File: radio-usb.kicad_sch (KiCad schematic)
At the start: 236 parts, among them J1 Barrel_Jack, J10 Conn_Coaxial, J11 ACJS-MHDRM, J12 ACJS-MHDRM, J2 miniUSB, J3 15EDGRC-3.5-03P-14, J4 DB9_Female, J5 EEP_EN, J6 Mini-DIN-6, J7 EDAC 690-008-221-904, J8 DB9_Male, J9 Conn_Coaxial, Q1 BC846C, Q2 BC846, Q3 BC846, Q4 BC846, Q5 BC856, SW1 SW_Push_DPDT, SW2 SW_SPDT, SW3 SW_SPDT, SW4 SW_DIP_x04, SW5 SW_DIP_x04, SW6 SW_DPDT_x2, SW7 SW_SPDT, U1 L7805, U10 AP2171W, U11 TLP2662, U12 TLP2662, U13 MAX3232, U14 93CxxC, U15 PCM2902, U16 MIC5209-3.6YS, U17 FT2232HL, U18 PC817, U19 CRIYCHLEY9000, U2 24LC04, U20 PC817, U21 PC817, U22 CRIYCHLEY9000, U23 LMV358, U3 APX809_810-xxSA, U4 AP22814AW5, U5 AP22814AW5, U6 USB2514B_Bi, U7 LM1117-3.3, U8 TBA 1-0511, U9 4069, X1 MAB5SH, Y1 24MHz, Y2 12MHz, Y3 12M

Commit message: daily
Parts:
- removed C43: 1u, Capacitor_SMD:C_0805_2012Metric_Pad1.18x1.45mm_HandSolder, symbol Device:C
- removed F1: Polyfuse 100mA, Resistor_SMD:R_1210_3225Metric_Pad1.30x2.65mm_HandSolder, symbol Device:Polyfuse
- removed R56: 0, Resistor_SMD:R_0805_2012Metric_Pad1.20x1.40mm_HandSolder, symbol Device:R
- removed R71, R72, R73, R74: 2k2, Resistor_SMD:R_0805_2012Metric_Pad1.20x1.40mm_HandSolder, symbol Device:R
- removed RV1: 10k, potentiometers:Potentiometer_SRpassives_1028F, symbol Device:R_Potentiometer
- removed U16: MIC5209-3.6YS, Package_TO_SOT_SMD:SOT-223-3_TabPin2, symbol MIC5209:MIC5209-3.3YS
- removed U23: LMV358, Package_SO:TSSOP-8_4.4x3mm_P0.65mm, symbol Amplifier_Operational:LMV358
- added R69: 0, Resistor_SMD:R_0603_1608Metric_Pad0.98x0.95mm_HandSolder, symbol Device:R_Small
- added R70: DNP, Resistor_SMD:R_0603_1608Metric_Pad0.98x0.95mm_HandSolder, symbol Device:R_Small
- added U23: LMV321IDBVR, Package_TO_SOT_SMD:SOT-23-5_HandSoldering, symbol Amplifier_Operational:LMV321
- R78: renamed from R76; footprint Resistor_SMD:R_0805_2012Metric_Pad1.20x1.40mm_HandSolder -> Resistor_SMD:R_0603_1608Metric_Pad0.98x0.95mm_HandSolder
- renumbered C42 to C43, C44 to C45, C45 to C46, C46 to C47, C47 to C48, C48 to C49, C49 to C50, C50 to C51, C51 to C52, C52 to C53, C53 to C54, C54 to C55, C55 to C56, C56 to C57, C57 to C58, C58 to C59, C59 to C60, C60 to C61, C61 to C62, C62 to C63, C63 to C64, C64 to C65, R44 to R42, R46 to R43, R42 to R44, R43 to R45, R45 to R46, R69 to R71, R70 to R72, R75 to R77, R77 to R79, R78 to R80, R79 to R81
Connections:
- net AUD_VBUS: now also U23.5 (V+)
- net GND: now also R70.1, U23.2 (V-)
- net PTT_CTRL: now also D17.1 (K), D18.1 (K), D19.1 (K), D20.1 (K)
- net VD: now also C23.1, L3.2
- net at C62.1, R77.2: now also U23.4
- net at R71.1: now also U23.1 (+)
- net at R67.2, R68.2, R77.1: now also U23.3 (-)
- net at J11.T: now also R69.1, R70.2
- net at U22.P$1: now also R69.2
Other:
- moved on the sheet: C49

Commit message: all components placed
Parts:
- removed C65: 100n, Capacitor_SMD:C_0805_2012Metric_Pad1.18x1.45mm_HandSolder, symbol Device:C
- R35, R36, R37: footprint Resistor_SMD:R_0805_2012Metric_Pad1.20x1.40mm_HandSolder -> Resistor_SMD:R_0603_1608Metric_Pad0.98x0.95mm_HandSolder
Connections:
- net DCDC_OUT: now reaches C20.1, C22.2, L3.1, U8.4 (+VOUT)
- net DCDC_IN: now reaches C18.1, C19.1, L2.2, U8.2 (+VIN)
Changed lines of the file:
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@@
     (effects (font (size 1.27 1.27)) (justify left bottom))
   )
+  (label "DCDC_IN" (at 125.984 134.366 0)
+    (effects (font (size 1.27 1.27)) (justify left bottom))
+  )
   (label "H_AUD_USBD-" (at 216.154 136.906 90)
     (effects (font (size 1.27 1.27)) (justify left bottom))
@@
     (effects (font (size 1.27 1.27)) (justify left bottom))
   )
+  (label "DCDC_OUT" (at 165.354 134.366 0)
+    (effects (font (size 1.27 1.27)) (justify left bottom))
+  )
   (label "DP2+" (at 178.308 79.502 0)
     (effects (font (size 1.27 1.27)) (justify left bottom))
@@
     (effects (font (size 1.27 1.27)) (justify right))
   )
-  (hierarchical_label "AUD_VBUS" (shape input) (at 392.938 152.654 90)
-    (effects (font (size 1.27 1.27)) (justify left))
-  )
   (hierarchical_label "CAT_UART_RX" (shape input) (at 197.866 191.516 0)
     (effects (font (size 1.27 1.27)) (justify left))
@@
     (property "Reference" "R35" (id 0) (at 179.07 17.78 90))
     (property "Value" "620" (id 1) (at 179.07 19.4111 90))
-    (property "Footprint" "Resistor_SMD:R_0805_2012Metric_Pad1.20x1.40mm_HandSolder" (id 2) (at 179.07 23.368 90)
+    (property "Footprint" "Resistor_SMD:R_0603_1608Metric_Pad0.98x0.95mm_HandSolder" (id 2) (at 179.07 23.368 90)
       (effects (font (size 1.27 1.27)) hide)
     )
@@
       (effects (font (size 1.27 1.27)) hide)
     )
-    (property "Footprint" "Resistor_SMD:R_0805_2012Metric_Pad1.20x1.40mm_HandSolder" (id 2) (at 179.07 28.448 90)
+    (property "Footprint" "Resistor_SMD:R_0603_1608Metric_Pad0.98x0.95mm_HandSolder" (id 2) (at 179.07 28.448 90)
       (effects (font (size 1.27 1.27)) hide)
     )
@@
     (pin "1")
   )
-  (symbol (lib_id "power:GND") (at 392.938 160.274 0) (mirror y) (unit 1)
-    (in_bom yes) (on_board yes)
-    (property "Reference" "#PWR0156" (id 0) (at 392.938 166.624 0)
-      (effects (font (size 1.27 1.27)) hide)
-    )
-    (property "Value" "GND" (id 1) (at 394.97 163.83 0)
-      (effects (font (size 1.27 1.27)) (justify left))
-    )
-    (property "Footprint" "" (id 2) (at 392.938 160.274 0)
-      (effects (font (size 1.27 1.27)) hide)
-    )
-    (property "Datasheet" "" (id 3) (at 392.938 160.274 0)
-      (effects (font (size 1.27 1.27)) hide)
-    )
-    (pin "1")
-  )
   (symbol (lib_id "Device:C_Small") (at 61.722 75.438 180) (unit 1)
     (in_bom yes) (on_board yes) (fields_autoplaced)
@@
       (effects (font (size 1.27 1.27)) hide)
     )
-    (property "Footprint" "Resistor_SMD:R_0805_2012Metric_Pad1.20x1.40mm_HandSolder" (id 2) (at 179.07 25.908 90)
+    (property "Footprint" "Resistor_SMD:R_0603_1608Metric_Pad0.98x0.95mm_HandSolder" (id 2) (at 179.07 25.908 90)
       (effects (font (size 1.27 1.27)) hide)
     )
@@
     (pin "2")
   )
-  (symbol (lib_id "Device:C") (at 392.938 156.464 0) (mirror y) (unit 1)
-    (in_bom yes) (on_board yes)
-    (property "Reference" "C65" (id 0) (at 389.89 154.686 0)
-      (effects (font (size 1.27 1.27)) (justify left))
-    )
-    (property "Value" "100n" (id 1) (at 390.906 157.734 0)
-      (effects (font (size 1.27 1.27)) (justify left))
-    )
-    (property "Footprint" "Capacitor_SMD:C_0805_2012Metric_Pad1.18x1.45mm_HandSolder" (id 2) (at 391.9728 160.274 0)
-      (effects (font (size 1.27 1.27)) hide)
-    )
-    (property "Datasheet" "~" (id 3) (at 392.938 156.464 0)
-      (effects (font (size 1.27 1.27)) hide)
-    )
-    (pin "1")
-    (pin "2")
-  )
   (symbol (lib_id "Device:R") (at 54.864 72.898 90) (unit 1)
     (in_bom yes) (on_board yes)
@@
       (reference "#PWR0155") (unit 1) (value "GND") (footprint "")
     )
-    (path "/d73cfa54-407e-467d-80c5-1fdb93348df7"
-      (reference "#PWR0156") (unit 1) (value "GND") (footprint "")
-    )
     (path "/f14d9d25-3ad4-4ba1-b81e-306fcdc3e5dd"
       (reference "C1") (unit 1) (value "100n") (footprint "Capacitor_SMD:C_0805_2012Metric_Pad1.18x1.45mm_HandSolder")
@@
       (reference "C64") (unit 1) (value "220u") (footprint "Capacitor_THT:CP_Radial_D6.3mm_P2.50mm")
     )
-    (path "/e1a1d8c1-19a5-45e1-ad5e-d6115bc273f7"
-      (reference "C65") (unit 1) (value "100n") (footprint "Capacitor_SMD:C_0805_2012Metric_Pad1.18x1.45mm_HandSolder")
-    )
     (path "/2b46b8ce-fbd7-4832-b43f-7c5a2c83b3b3"
       (reference "D1") (unit 1) (value "LED_ACTIVE") (footprint "LED_SMD:LED_0805_2012Metric_Pad1.15x1.40mm_HandSolder")
@@
     )
     (path "/6c4d68f5-d716-44a9-aeb7-6ba243282166"
-      (reference "R35") (unit 1) (value "620") (footprint "Resistor_SMD:R_0805_2012Metric_Pad1.20x1.40mm_HandSolder")
+      (reference "R35") (unit 1) (value "620") (footprint "Resistor_SMD:R_0603_1608Metric_Pad0.98x0.95mm_HandSolder")
     )
     (path "/d8665dd2-e80d-41da-8e8d-aef27598c8ad"
-      (reference "R36") (unit 1) (value "620") (footprint "Resistor_SMD:R_0805_2012Metric_Pad1.20x1.40mm_HandSolder")
+      (reference "R36") (unit 1) (value "620") (footprint "Resistor_SMD:R_0603_1608Metric_Pad0.98x0.95mm_HandSolder")
     )
     (path "/9cad4074-74b4-4ae9-b371-1f5200a781e5"
-      (reference "R37") (unit 1) (value "620") (footprint "Resistor_SMD:R_0805_2012Metric_Pad1.20x1.40mm_HandSolder")
+      (reference "R37") (unit 1) (value "620") (footprint "Resistor_SMD:R_0603_1608Metric_Pad0.98x0.95mm_HandSolder")
     )
     (path "/2695bdf0-efc1-447a-8be3-1d0a7f2f5f82"

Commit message: more pcb traces routing
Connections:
- net +3V3: no longer R49.2, R51.2, R52.2, U14.6 (ORG), U14.8 (VCC)
- net SER_VCCIO: now also R49.2, R51.2, R52.2, U14.6 (ORG), U14.8 (VCC)
- net AF_FRM_RADIO_PREINS: now reaches J11.T, R69.1, R70.2
- net AUD_FRM_RADIO renamed AF_FRM_RADIO
- net AUD_TO_RADIO renamed AF_TO_RADIO
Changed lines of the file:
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@@
   (junction (at 333.248 115.316) (diameter 0) (color 0 0 0 0)
   )
+  (junction (at 231.648 96.266) (diameter 0) (color 0 0 0 0)
+  )
   (junction (at 183.642 267.208) (diameter 0) (color 0 0 0 0)
   )
@@
   (junction (at 330.708 117.856) (diameter 0) (color 0 0 0 0)
   )
+  (junction (at 351.028 218.694) (diameter 0) (color 0 0 0 0)
+  )
   (junction (at 324.358 175.006) (diameter 0) (color 0 0 0 0)
   )
@@
   (junction (at 288.544 141.986) (diameter 0) (color 0 0 0 0)
   )
-  (junction (at 231.648 96.266) (diameter 0) (color 0 0 0 0)
-  )
   (junction (at 17.653 137.668) (diameter 0) (color 0 0 0 0)
   )
@@
     (stroke (width 0) (type default) (color 0 0 0 0))
   )
-  (wire (pts (xy 351.028 218.694) (xy 351.028 217.424))
+  (wire (pts (xy 351.028 217.424) (xy 351.028 218.694))
     (stroke (width 0) (type default) (color 0 0 0 0))
   )
@@
     (stroke (width 0) (type default) (color 0 0 0 0))
   )
-  (wire (pts (xy 240.284 248.92) (xy 245.11 248.92))
-    (stroke (width 0) (type default) (color 0 0 0 0))
-  )
   (wire (pts (xy 184.912 54.61) (xy 184.912 66.802))
     (stroke (width 0) (type default) (color 0 0 0 0))
@@
     (stroke (width 0) (type default) (color 0 0 0 0))
   )
-  (wire (pts (xy 231.648 96.012) (xy 231.648 96.266))
+  (wire (pts (xy 240.284 248.92) (xy 245.11 248.92))
     (stroke (width 0) (type default) (color 0 0 0 0))
   )
@@
     (stroke (width 0) (type default) (color 0 0 0 0))
   )
+  (wire (pts (xy 351.028 218.694) (xy 351.028 224.79))
+    (stroke (width 0) (type default) (color 0 0 0 0))
+  )
   (wire (pts (xy 283.972 19.05) (xy 286.004 19.05))
     (stroke (width 0) (type default) (color 0 0 0 0))
@@
     (stroke (width 0) (type default) (color 0 0 0 0))
   )
+  (wire (pts (xy 231.648 96.266) (xy 231.648 98.806))
+    (stroke (width 0) (type default) (color 0 0 0 0))
+  )
   (wire (pts (xy 109.982 179.578) (xy 109.982 179.832))
     (stroke (width 0) (type default) (color 0 0 0 0))
@@
     (stroke (width 0) (type default) (color 0 0 0 0))
   )
+  (wire (pts (xy 232.664 93.726) (xy 231.648 93.726))
+    (stroke (width 0) (type default) (color 0 0 0 0))
+  )
   (wire (pts (xy 385.318 40.386) (xy 385.318 32.766))
     (stroke (width 0) (type default) (color 0 0 0 0))
@@
     (stroke (width 0) (type default) (color 0 0 0 0))
   )
-  (wire (pts (xy 231.648 96.266) (xy 231.648 98.806))
+  (wire (pts (xy 231.648 93.726) (xy 231.648 96.266))
     (stroke (width 0) (type default) (color 0 0 0 0))
   )
@@
     (effects (font (size 1.27 1.27)) (justify left bottom))
   )
-  (global_label "AUD_FRM_RADIO" (shape input) (at 30.734 271.272 180) (fields_autoplaced)
+  (global_label "AF_FRM_RADIO" (shape input) (at 30.734 271.272 180) (fields_autoplaced)
     (effects (font (size 1.27 1.27)) (justify right))
-    (property "Intersheet References" "${INTERSHEET_REFS}" (id 0) (at 13.3228 271.3514 0)
+    (property "Intersheet References" "${INTERSHEET_REFS}" (id 0) (at 14.8347 271.1926 0)
       (effects (font (size 1.27 1.27)) (justify right) hide)
     )
   )
-  (global_label "AUD_TO_RADIO" (shape input) (at 97.028 268.732 90) (fields_autoplaced)
+  (global_label "AF_TO_RADIO" (shape input) (at 97.028 268.732 90) (fields_autoplaced)
     (effects (font (size 1.27 1.27)) (justify left))
-    (property "Intersheet References" "${INTERSHEET_REFS}" (id 0) (at 97.1074 252.8327 90)
+    (property "Intersheet References" "${INTERSHEET_REFS}" (id 0) (at 96.9486 254.3446 90)
       (effects (font (size 1.27 1.27)) (justify left) hide)
     )
@@
     )
   )
-  (global_label "AUD_TO_RADIO" (shape input) (at 350.52 189.738 180) (fields_autoplaced)
+  (global_label "AF_TO_RADIO" (shape input) (at 350.52 189.738 180) (fields_autoplaced)
     (effects (font (size 1.27 1.27)) (justify right))
-    (property "Intersheet References" "${INTERSHEET_REFS}" (id 0) (at 334.6207 189.6586 0)
+    (property "Intersheet References" "${INTERSHEET_REFS}" (id 0) (at 336.1326 189.6586 0)
       (effects (font (size 1.27 1.27)) (justify right) hide)
     )
@@
     )
   )
-  (global_label "AUD_FRM_RADIO" (shape input) (at 390.144 213.614 0) (fields_autoplaced)
+  (global_label "AF_FRM_RADIO" (shape input) (at 390.144 213.614 0) (fields_autoplaced)
     (effects (font (size 1.27 1.27)) (justify left))
-    (property "Intersheet References" "${INTERSHEET_REFS}" (id 0) (at 407.5552 213.5346 0)
+    (property "Intersheet References" "${INTERSHEET_REFS}" (id 0) (at 406.0433 213.5346 0)
       (effects (font (size 1.27 1.27)) (justify left) hide)
     )
   )
-  (global_label "AUD_FRM_RADIO" (shape input) (at 100.33 268.732 90) (fields_autoplaced)
+  (global_label "AF_FRM_RADIO" (shape input) (at 100.33 268.732 90) (fields_autoplaced)
     (effects (font (size 1.27 1.27)) (justify left))
-    (property "Intersheet References" "${INTERSHEET_REFS}" (id 0) (at 100.2506 251.3208 90)
+    (property "Intersheet References" "${INTERSHEET_REFS}" (id 0) (at 100.2506 252.8327 90)
       (effects (font (size 1.27 1.27)) (justify left) hide)
     )
@@
     )
   )
-  (global_label "AUD_TO_RADIO" (shape input) (at 91.44 243.078 0) (fields_autoplaced)
+  (global_label "AF_TO_RADIO" (shape input) (at 91.44 243.078 0) (fields_autoplaced)
     (effects (font (size 1.27 1.27)) (justify left))
-    (property "Intersheet References" "${INTERSHEET_REFS}" (id 0) (at 107.3393 243.1574 0)
+    (property "Intersheet References" "${INTERSHEET_REFS}" (id 0) (at 105.8274 242.9986 0)
       (effects (font (size 1.27 1.27)) (justify left) hide)
     )
@@
     )
   )
-  (global_label "AUD_TO_RADIO" (shape input) (at 30.734 281.432 180) (fields_autoplaced)
+  (global_label "AF_TO_RADIO" (shape input) (at 30.734 281.432 180) (fields_autoplaced)
     (effects (font (size 1.27 1.27)) (justify right))
-    (property "Intersheet References" "${INTERSHEET_REFS}" (id 0) (at 14.8347 281.3526 0)
+    (property "Intersheet References" "${INTERSHEET_REFS}" (id 0) (at 16.3466 281.3526 0)
       (effects (font (size 1.27 1.27)) (justify right) hide)
     )
@@
     )
   )
-  (global_label "AUD_FRM_RADIO" (shape input) (at 87.122 226.06 0) (fields_autoplaced)
+  (global_label "AF_FRM_RADIO" (shape input) (at 87.122 226.06 0) (fields_autoplaced)
     (effects (font (size 1.27 1.27)) (justify left))
-    (property "Intersheet References" "${INTERSHEET_REFS}" (id 0) (at 104.5332 225.9806 0)
+    (property "Intersheet References" "${INTERSHEET_REFS}" (id 0) (at 103.0213 225.9806 0)
       (effects (font (size 1.27 1.27)) (justify left) hide)
     )
@@
     (effects (font (size 1.27 1.27)) (justify left))
   )
+  (hierarchical_label "SER_VCCIO" (shape input) (at 232.664 93.726 0)
+    (effects (font (size 1.27 1.27)) (justify left))
+  )
   (hierarchical_label "PTT_CTRL" (shape input) (at 366.522 58.674 0)
     (effects (font (size 1.27 1.27)) (justify left))
@@
     (effects (font (size 1.27 1.27)) (justify right))
   )
+  (hierarchical_label "SER_VCCIO" (shape input) (at 218.948 104.394 90)
+    (effects (font (size 1.27 1.27)) (justify left))
+  )
   (hierarchical_label "TTL_RX_2" (shape input) (at 181.356 262.128 0)
     (effects (font (size 1.27 1.27)) (justify left))
@@
     (effects (font (size 1.27 1.27)) (justify right))
   )
+  (hierarchical_label "AF_FRM_RADIO_PREINS" (shape input) (at 351.028 224.79 270)
+    (effects (font (size 1.27 1.27)) (justify right))
+  )
   (hierarchical_label "TTL_TX_2" (shape input) (at 200.914 162.052 90)
     (effects (font (size 1.27 1.27)) (justify left))
@@
     (pin "1")
   )
-  (symbol (lib_id "power:+3V3") (at 218.948 104.394 0) (unit 1)
-    (in_bom yes) (on_board yes)
-    (property "Reference" "#PWR098" (id 0) (at 218.948 108.204 0)
-      (effects (font (size 1.27 1.27)) hide)
-    )
-    (property "Value" "+3V3" (id 1) (at 216.154 100.584 0)
-      (effects (font (size 1.27 1.27)) (justify left))
-    )
-    (property "Footprint" "" (id 2) (at 218.948 104.394 0)
-      (effects (font (size 1.27 1.27)) hide)
-    )
-    (property "Datasheet" "" (id 3) (at 218.948 104.394 0)
-      (effects (font (size 1.27 1.27)) hide)
-    )
-    (pin "1")
-  )
   (symbol (lib_id "Switch:SW_DPDT_x2") (at 374.904 86.614 0) (unit 1)
     (in_bom yes) (on_board yes) (fields_autoplaced)
@@
     (pin "3")
   )
-  (symbol (lib_id "power:+3V3") (at 231.648 96.012 0) (unit 1)
-    (in_bom yes) (on_board yes)
-    (property "Reference" "#PWR0102" (id 0) (at 231.648 99.822 0)
-      (effects (font (size 1.27 1.27)) hide)
-    )
-    (property "Value" "+3V3" (id 1) (at 225.552 94.488 0)
-      (effects (font (size 1.27 1.27)) (justify left))
-    )
-    (property "Footprint" "" (id 2) (at 231.648 96.012 0)
-      (effects (font (size 1.27 1.27)) hide)
-    )
-    (property "Datasheet" "" (id 3) (at 231.648 96.012 0)
-      (effects (font (size 1.27 1.27)) hide)
-    )
-    (pin "1")
-  )
   (symbol (lib_id "power:VBUS") (at 75.946 154.94 0) (unit 1)
     (in_bom yes) (on_board yes) (fields_autoplaced)
@@
       (reference "#PWR097") (unit 1) (value "GND") (footprint "")
     )
-    (path "/18792c27-b5ab-4036-ae90-f3e85ac59076"
-      (reference "#PWR098") (unit 1) (value "+3V3") (footprint "")
-    )
     (path "/5d6bbbd9-867f-4762-a561-c8ddddfd7960"
       (reference "#PWR099") (unit 1) (value "GNDREF") (footprint "")
@@
       (reference "#PWR0101") (unit 1) (value "GND") (footprint "")
     )
-    (path "/1a907893-a486-4da1-bfbd-170b67f12148"
-      (reference "#PWR0102") (unit 1) (value "+3V3") (footprint "")
-    )
     (path "/152a0aef-d257-46c9-a9a8-356c44fa4c73"

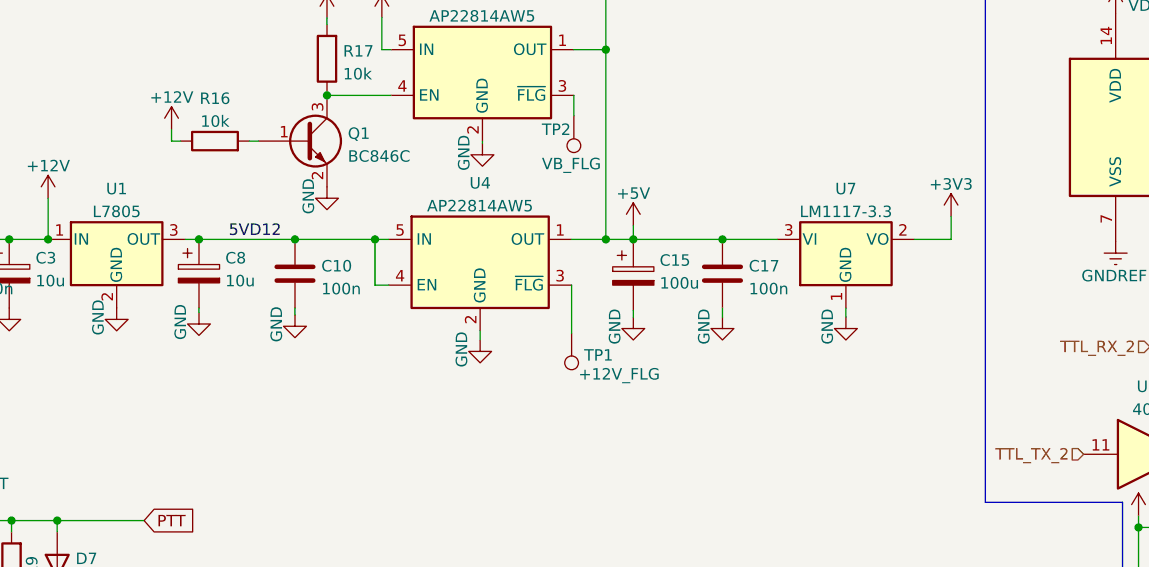
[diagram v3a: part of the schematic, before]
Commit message: everything but ground poluygon and fixed bourns trafo pinout
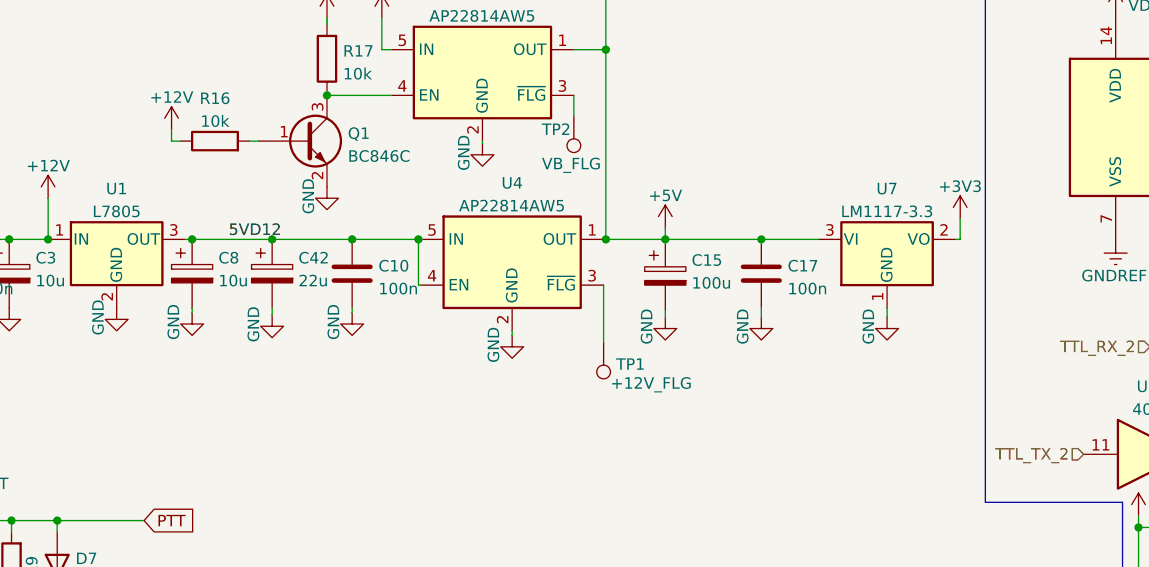
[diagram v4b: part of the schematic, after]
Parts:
- added C42: 22u, Capacitor_Tantalum_SMD:CP_EIA-3216-18_Kemet-A_Pad1.58x1.35mm_HandSolder, symbol Device:C_Polarized
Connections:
- net 5VD12: now also C42.1
- net GND: now also C42.2
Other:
- moved on the sheet: C10, C15, C17, C8, TP1, U4, U7
